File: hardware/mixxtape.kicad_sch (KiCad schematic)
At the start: 72 parts, among them J1 USB-C-16P, J2 JST-PH-2 (DNP), J3 CASTELLATED, SW1 REC, SW2 PLAY, SW3 TRACK, SW4 MODE, U1 ESP32-WROOM-32E-N4, U2 MSM261S4030H0R, U3 W25Q128JVSIQ, U4 AMS1117-3.3, U5 TP4056 (DNP), U6 CH340N, U7 USBLC6-2SC6, U8 SN74AHCT1G125

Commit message: hardware: USB-C power-only, pogo jig, CC sense, DNP microSD
- Remove CH340N + USBLC6 and the USB data path; USB-C is power only.
  Resolves the CH340N-has-no-DTR problem by deletion.
- Remove the castellated hacker header; add J5, six bare pogo pads
  (3V3/GND/EN/IO0/TX/RX). The jig carries the bridge and auto-program
  transistors.
- Add CC1/CC2 sensing through 10k to ADC1 (GPIO36/39) so firmware can
  read the source current advertisement and raise the LED brightness cap.
- Add J4 microSD (TF-01A, C91145) + R9 pullup as footprint-only DNP,
  SPI mode sharing VSPI; CS=IO22, card-detect=IO32.
- Add SN74AHCT1G125 (C7484) level shifter U8 for the WS2812 chain.
- docs/prior-art.md: eleven cassette-form-factor projects, incl. the
  Digisette Duo-Aria (2000), the only prior device with record+playback
  in the shell.
- docs/firmware-plan.md: agent handoff plan; ESP-IDF locked (Zephyr
  rejected: BLE-first stack, no supported A2DP path on ESP32).

ERC: 0 errors.

Co-Authored-By: Claude Fable 5 <noreply@anthropic.com>
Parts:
- removed C10, C3, C4: 100nF, mixxtape_parts:C0402, symbol mixxtape_parts:CL05B104KO5NNNC
- removed J3: CASTELLATED, symbol mixxtape_local:CONN_10
- removed U6: CH340N, mixxtape_parts:SOP-8_L5.0-W4.0-P1.27-LS6.0-BL, symbol mixxtape_parts:CH340N
- removed U7: USBLC6-2SC6, mixxtape_parts:SOT-23-6_L2.9-W1.6-P0.95-LS2.8-BL, symbol mixxtape_parts:USBLC6-2SC6
- added J4: microSD (DNP), mixxtape_parts:TF-SMD_TF-01A, symbol mixxtape_parts:TF-01A
- added J5: PROG-JIG, symbol mixxtape_local:CONN_6
- added R10, R11: 10k, mixxtape_parts:R0603, symbol mixxtape_parts:0603WAF1002T5E
- added R9: 10k (DNP), mixxtape_parts:R0603, symbol mixxtape_parts:0603WAF1002T5E
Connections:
- net 3V3: now also J4.4 (VDD), J5.1, R9.1
- net BTN_REC: now also J5.4
- net CC1: now also R10.1
- net CC2: now also R11.1
- net EN: now also J5.3
- net GND: now also J4.10 (GND), J4.11 (GND), J4.12 (GND), J4.13 (GND), J4.6 (VSS), J5.2
- net SPI_CLK: now also J4.5 (CLK(SCLK))
- net SPI_MISO: now also J4.7 (DAT0(D0))
- net SPI_MOSI: now also J4.3 (CMD(DI))
- net UART_RX: now also J5.6
- net UART_TX: now also J5.5
- net SD_CS_N: now reaches U1.36 (IO22)
- net SD_CS_N: now also J4.2 (CDDAT3(CS)), R9.2
- net CC1_SENSE: now reaches U1.4 (SENSOR_VP)
- net CC1_SENSE: now also R10.2
- net CC2_SENSE: now reaches U1.5 (SENSOR_VN)
- net CC2_SENSE: now also R11.2
- net SD_DETECT: now reaches U1.8 (IO32)
- net SD_DETECT: now also J4.9 (CD)
- net GPIO13: no longer names the net of U1.16 (IO13)
- net GPIO14: no longer names the net of U1.13 (IO14)
- net USB_DN_C: no longer names the net of J1.A7 (DN1)
- net USB_DN_C: no longer J1.B7 (DN2)
- net USB_DP_C: no longer names the net of J1.A6 (DP1)
- net USB_DP_C: no longer J1.B6 (DP2)
- no-connect marks 22 -> 26
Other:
- note added: "CC SENSE: firmware reads CC1/CC2 on ADC1 (GPIO36/39) to detect the"
- note added: "DNP: TP4056+JST battery, IO34 battery-sense divider, IO35 line-in (jack needs Steven),"
- note added: "ESP32 (GPIO map: docs/cassette-recorder-agent-brief.md sec.5 + docs/firmware-plan.md)"
- note added: "J4 microSD studio-edition option (CS=IO22, detect=IO32, shares VSPI; CD needs internal pullup)."
- note added: "MICROSD (DNP)"
- note added: "PROG JIG: 6 pogo pads. Jig carries USB-UART + EN/IO0 auto-program drivers."
- note added: "USB source's current advertisement; LED cap stays 500mA-safe by default."
- note added: "USB-C: POWER ONLY + CC SENSE (no USB data on board)"
- note removed: "Alternative: CH340C/CH343 with DTR. Q1/Q2 omitted until decided."
- note removed: "DNP: TP4056+JST battery, IO34 battery-sense divider, IO35 line-in (jack needs Steven)."
- note removed: "ESP32 (GPIO map: docs/cassette-recorder-agent-brief.md sec.5)"
- note removed: "Fitted: cap-coupled RTS reset (C10) + hold-REC(IO0)-at-plug-in to enter bootloader."
- note removed: "HACKER HEADER: 10 castellated pads"
- note removed: "TODO: CH340N has RTS# only, no DTR - BOM's S8050 auto-reset pair needs both signals."
- note removed: "USB-C + ESD + USB-UART"

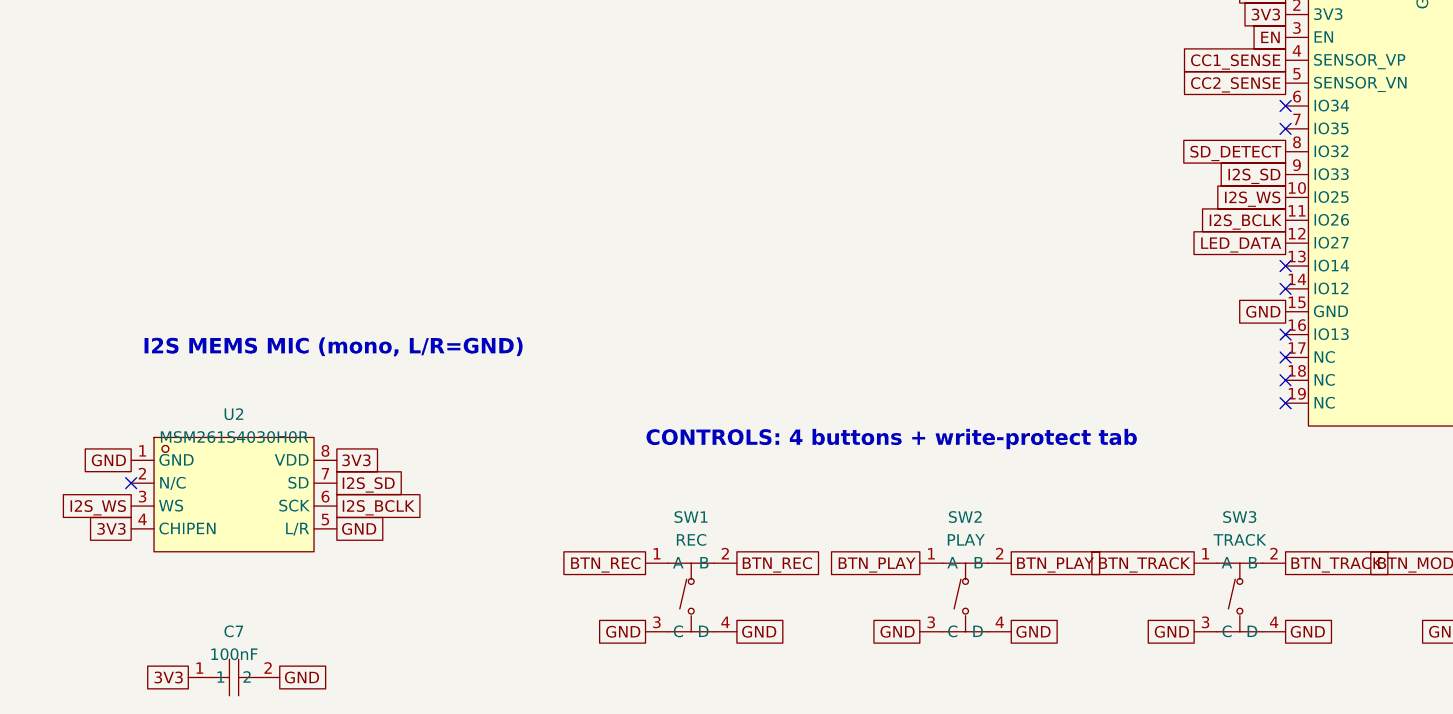
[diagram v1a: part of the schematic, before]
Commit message: mic: move to MSM261DHT006 (PDM) across hardware and firmware
Replaces MSM261S4030H0R, which is at zero stock. Acoustically an equal
swap: identical -26 dBFS sensitivity, same 1.6-3.6 V range, same 4x3 mm
LGA-8 outline, 1 dB less SNR and 2 dB better acoustic overload, at $0.45
against $1.61.

This was a schematic change rather than a part-number swap, because the
pinout is completely different: pin 1 is VDD where the old part had GND,
L/R moves to pin 2, and pins 5-8 are all GND. New footprint fetched from
EasyEDA and verified against the datasheet pin table.

Interface moves from I2S to PDM. That is two wires instead of three, so
GPIO26 is now free; GPIO25 carries the PDM clock and GPIO33 the data. The
ESP32's I2S peripheral does PDM receive and decimation in hardware, so
nothing downstream of the capture task changes.

One trap worth recording, and it is in board.h next to the constant: the
PDM downsample ratio must be 64, not 128. PDM clock is sample rate times
ratio, and 44100 x 128 = 5.64 MHz is above this microphone's 4.8 MHz
maximum. 64 gives 2.8224 MHz, comfortably inside its window.

Board cost falls to $9.85 from $11.01. ERC 0 errors, DRC 0 violations,
11 host suites green.

Co-Authored-By: Claude Opus 5 <noreply@anthropic.com>
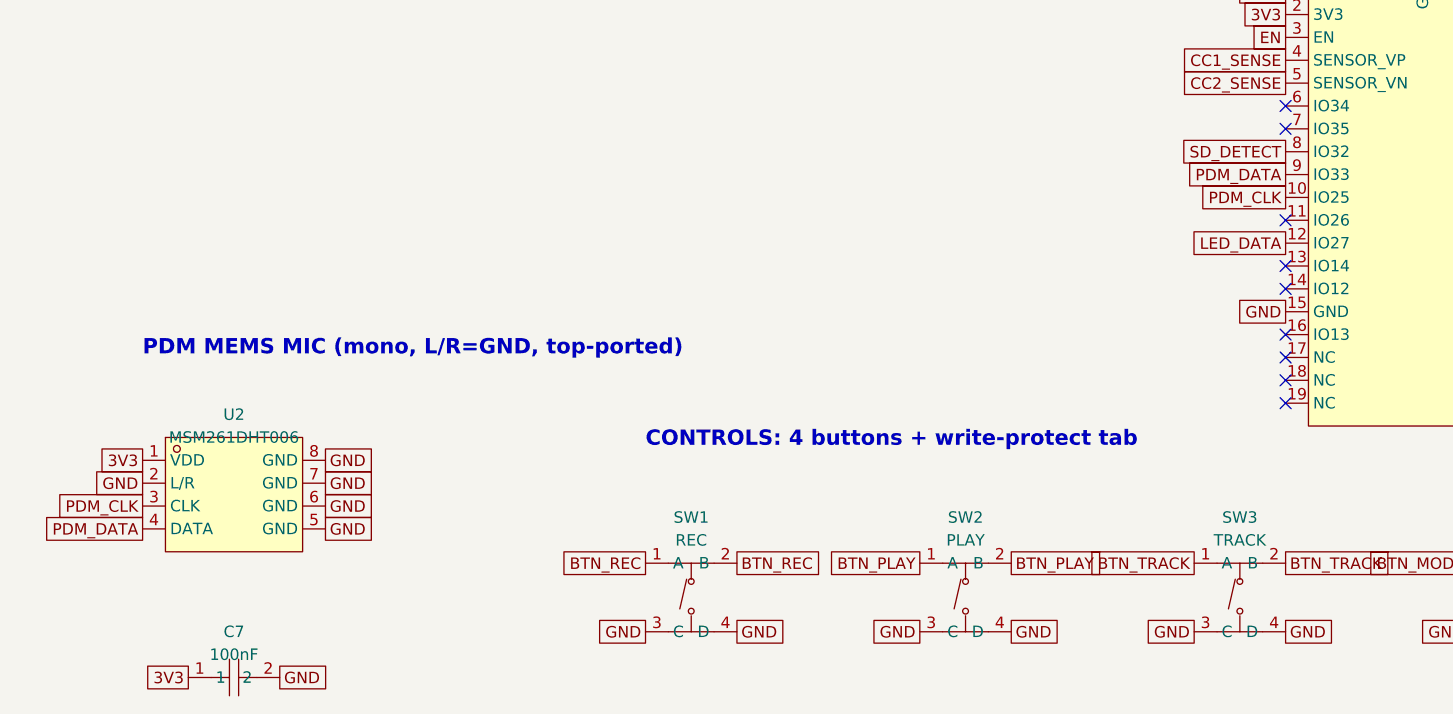
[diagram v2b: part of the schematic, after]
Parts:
- removed U2: MSM261S4030H0R, mixxtape_parts:MIC-SMD_8P-L4.0-W3.0-P1.00-BR, symbol mixxtape_parts:MSM261S4030H0R
- added U2: MSM261DHT006, mixxtape_parts:LGA-8_L4.0-W3.0-R_WMM7040DT0, symbol mixxtape_parts:MSM261DHT006
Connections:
- net 3V3: now also U2.1 (VDD)
- net GND: now also U2.2 (L/R), U2.5 (GND), U2.6 (GND), U2.7 (GND), U2.8 (GND)
- net I2S_BCLK: no longer names the net of U1.11 (IO26)
- net I2S_SD renamed PDM_DATA
- net PDM_DATA: now also U2.4 (DATA)
- net I2S_WS renamed PDM_CLK
- net PDM_CLK: now also U2.3 (CLK)
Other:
- note added: "PDM MEMS MIC (mono, L/R=GND, top-ported)"
- note removed: "I2S MEMS MIC (mono, L/R=GND)"

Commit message: hardware: pre-routing review — outline, pin types, TAB1, battery removal
Checked every footprint and every net before routing starts.

The board outline was self-intersecting and would have failed CAM. The
write-protect tab's two slots were drawn as closed rectangles lying on top
of the top edge instead of cut into it, so the edge ran straight through
both. Split the top edge into three spans and removed the slot mouths.

Every symbol pin now has a real electrical type. easyeda2kicad types every
pin "unspecified", which silently disables the checks that matter, so ERC
was reporting 191 warnings of one meaningless class and nothing else. 109
pins retyped from the datasheets, in the schematic and in the library so a
library update cannot undo it. That immediately found three genuine faults:
U4's two VOUT pins and J1's paired VBUS and GND pins each read as two power
outputs fighting over one rail. ERC is now 0.

TAB1 had no footprint, so TAB_SENSE would have read permanently low. Added
TAB_BREAKOFF_LINK, a two-pad net tie on the break-off tongue.

The battery section is removed. U5, J2 and R8 were always DNP and could
never have worked: a lithium cell at 3.0-4.2 V cannot feed an AMS1117 that
needs 1.1-1.3 V of headroom, and the LEDs sit on the 5 V USB rail besides.

Datasheet-driven part changes: C9 100 nF -> 1 uF on EN, which is what the
ESP32-WROOM-32E datasheet asks for, and a new R12 100 R in the microphone's
supply per figure 1 of the MSM261DHT006 datasheet, with C7 moved onto
MIC_VDD so the two actually form a filter.

Also: three mounting holes, four zero-annulus locating pegs made non-plated,
a DRC rule scoping J1's 0.10 mm internal pad spacing, and corrected datasheet
links (the LEDs pointed at Worldsemi while the fitted part is XINGLIGHT).

Verified: ERC 0, DRC clean apart from the 130 unrouted nets, every
footprint's pads reconcile with its symbol's pins, and every board pad
agrees with the schematic netlist.

Co-Authored-By: Claude Opus 5 <noreply@anthropic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
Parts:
- removed C9: 100nF, mixxtape_parts:C0402, symbol mixxtape_parts:CL05B104KO5NNNC
- removed J2: JST-PH-2 (DNP), symbol mixxtape_local:CONN_2
- removed R8: 10k (DNP), mixxtape_parts:R0603, symbol mixxtape_parts:0603WAF1002T5E
- removed U5: TP4056 (DNP), mixxtape_parts:ESOP-8_L4.9-W3.9-P1.27-LS6.0-BL-EP, symbol mixxtape_parts:TP4056
- added C9: 1uF, mixxtape_parts:C0402, symbol mixxtape_parts:CL05A105KO5NNNC
- added R12: 100R, mixxtape_parts:R0402, symbol mixxtape_parts:0402WGF1000TCE
- J5: footprint (none) -> mixxtape_local:PROG_JIG_6PAD
- TAB1: footprint (none) -> mixxtape_local:TAB_BREAKOFF_LINK
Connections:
- net 3V3: now also R12.1; no longer C7.1, U2.1 (VDD)
- net EN: now also C9.1
- net GND: now also C9.2
- new net MIC_VDD: C7.1, R12.2, U2.1 (VDD)
- no-connect marks 26 -> 24

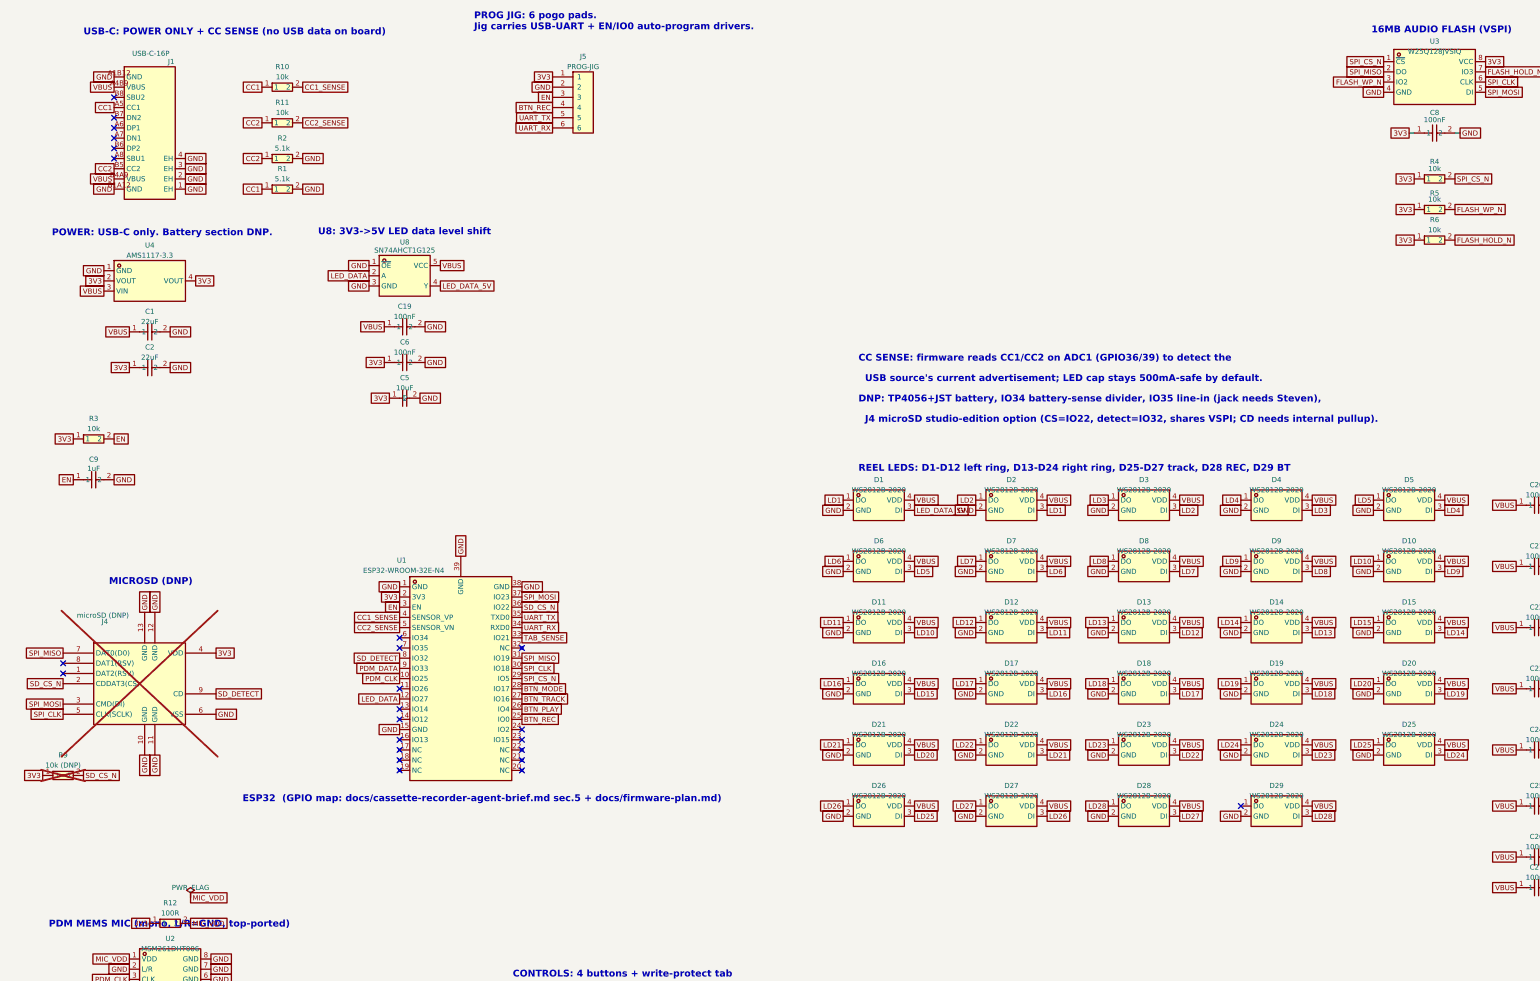
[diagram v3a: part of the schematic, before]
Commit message: hardware+firmware: flash second-sourced, passives on 0402, ERC actually clean
Flash: U3 moves from Winbond W25Q128JVSIQ (C97521) to GigaDevice
GD25Q128ESIG (C2758105), $2.2557 -> $1.3348 at a run of 20, net $15.41
after the Extended setup fee. Land patterns agree to 0.02 mm and the
command set and 256 B / 4 KiB / 64 KiB geometry are identical, so neither
the layout nor the storage design changes. The only difference is the
JEDEC manufacturer byte, so rather than move the hard-coded constant both
the driver and the factory test now accept either id and log which part
was found - C97521 stays a genuine drop-in second source. Host tests 11/11.

Passives: the eight 10k resistors move R0603 -> R0402, cheaper as well as
smaller, no traces broken. C1/C2 stay 0805 because the only Basic 10uF in
0402 is 6.3 V and C1 sits on the 5 V USB rail, where derating would leave
~2 uF of the nominal 10 for 29 LEDs.

ERC: three dangling 1.27 mm wire stubs left behind by the touch-pad
removal. These had been reported as clean because the report being read
was stale - kicad-cli writes its report relative to the working directory,
not next to the board. Both locations are now gitignored and the tracked
copy is deleted. ERC is now 0 errors, 0 warnings.

Checklist: the case-fit test passed against a real plastic case, which
retires the largest mechanical unknown. Testing against other brands stays
open. Also corrected the instruction to re-run gen_layout.py, which would
have rebuilt the original 100.33 mm outline and discarded the trim to
99.50 mm along with every route since.

fab/ now holds the JLCPCB upload package and its README.

Board cost $9.41 -> $8.62.

Co-Authored-By: Claude Opus 5 <noreply@anthropic.com>
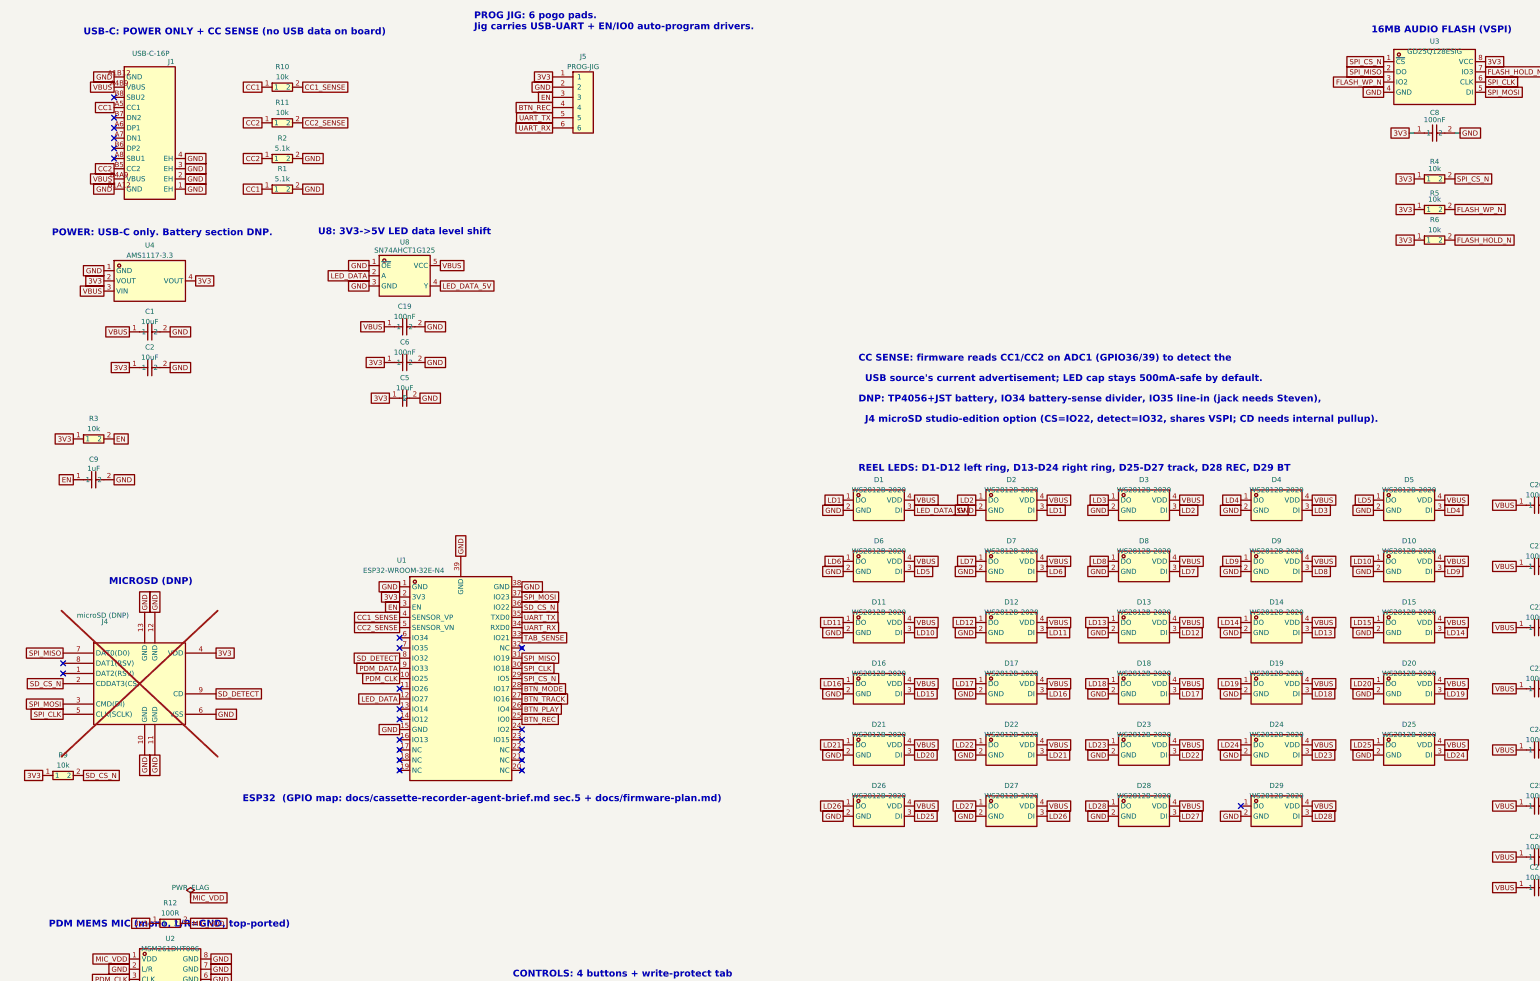
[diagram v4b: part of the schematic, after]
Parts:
- C1, C2: value 22uF -> 10uF; symbol mixxtape_parts:CL21A226MAQNNNE -> mixxtape_parts:CL21A106KAYNNNE; LCSC C45783 -> C15850
- C9: symbol mixxtape_parts:CL05A105KO5NNNC -> mixxtape_parts:CL05A105KA5NQNC; LCSC C29266 -> C52923
- R10, R11, R3, R4, R5, R6, R7: footprint mixxtape_parts:R0603 -> mixxtape_parts:R0402; symbol mixxtape_parts:0603WAF1002T5E -> mixxtape_parts:0402WGF1002TCE; LCSC C25804 -> C25744
- R9: value 10k (DNP) -> 10k; footprint mixxtape_parts:R0603 -> mixxtape_parts:R0402; symbol mixxtape_parts:0603WAF1002T5E -> mixxtape_parts:0402WGF1002TCE; LCSC C25804 -> C25744; now fitted
- U3: value W25Q128JVSIQ -> GD25Q128ESIG; symbol mixxtape_parts:W25Q128JVSIQTR -> mixxtape_parts:GD25Q128ESIG; LCSC C97521 -> C2758105
